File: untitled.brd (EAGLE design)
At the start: 100 x 80 mm, 8 parts

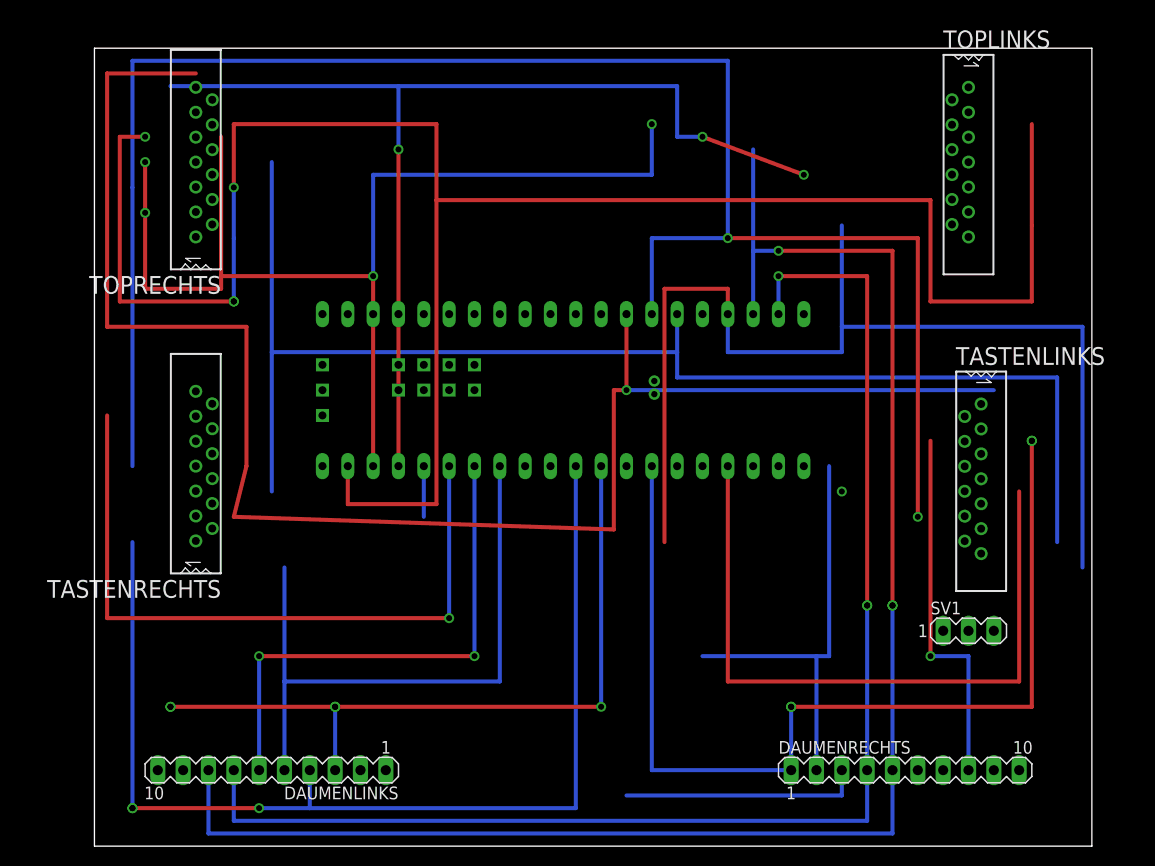
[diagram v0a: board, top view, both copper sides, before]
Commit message: first autorouted version
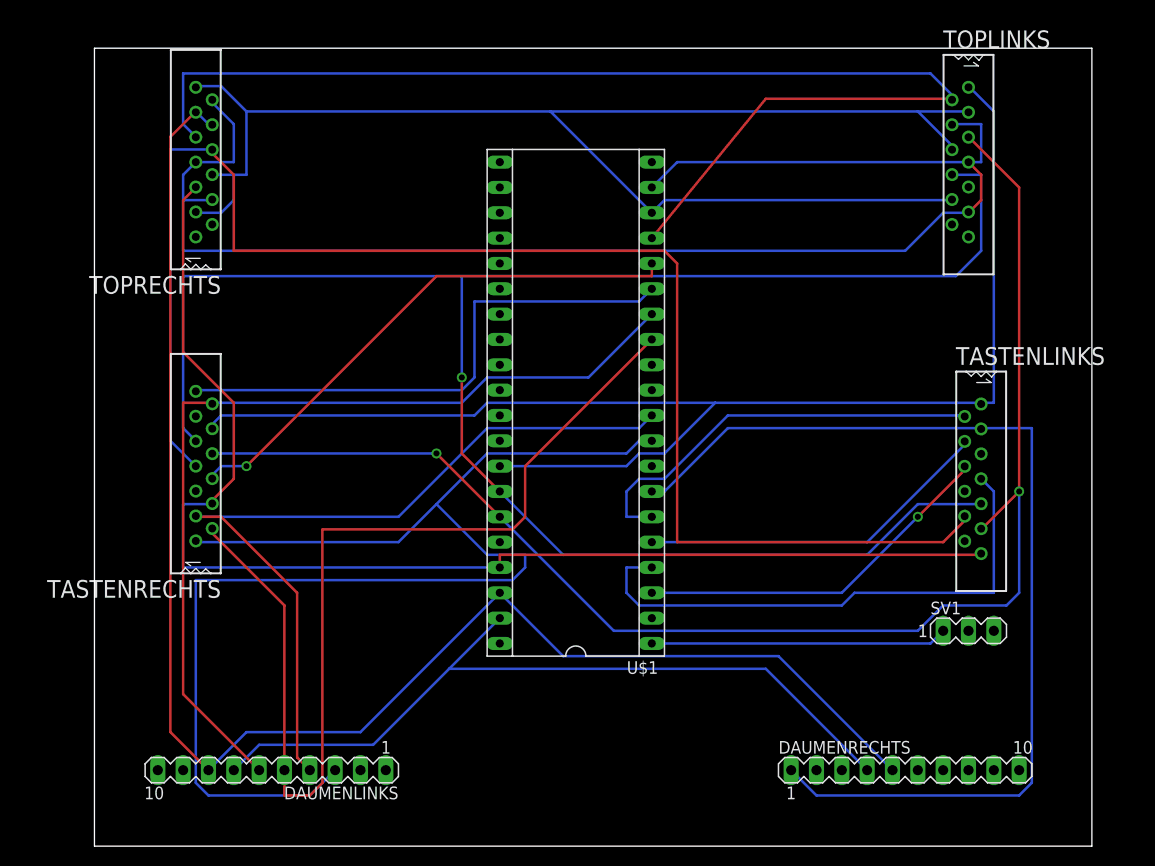
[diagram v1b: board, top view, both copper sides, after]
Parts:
- moved U$1 1.80 mm to (48.3, 44.5), flipped to the top, turned to 90 degrees
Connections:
- net GND: no longer U$1.GND2
- net VCC: no longer U$1.5V
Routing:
- net N$2: track 0.00 -> 152.1 mm
- net D6: track 73.7 -> 131.7 mm, vias 3 -> 0
- net B6: track 135.9 -> 79.1 mm, vias 2 -> 0
- net C6: track 207.0 -> 151.4 mm, vias 3 -> 0
- net C3: track 5.08 -> 54.5 mm, vias 0 -> 1
- net D2: track 43.2 -> 0.00 mm
- net N$16: track 0.00 -> 42.9 mm
- net C0: track 63.5 -> 103.8 mm
- net C1: track 52.1 -> 91.4 mm, vias 2 -> 0
- net N$18: track 0.00 -> 37.4 mm, vias 0 -> 1
- net D3: track 36.8 -> 0.00 mm, vias 1 -> 0
- net N$17: track 0.00 -> 36.3 mm
- net C5: track 113.0 -> 147.7 mm, vias 4 -> 0
- net N$14: track 0.00 -> 29.7 mm
- net B0: track 165.3 -> 137.4 mm, vias 1 -> 0
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
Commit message: board grid set to 1.25mm
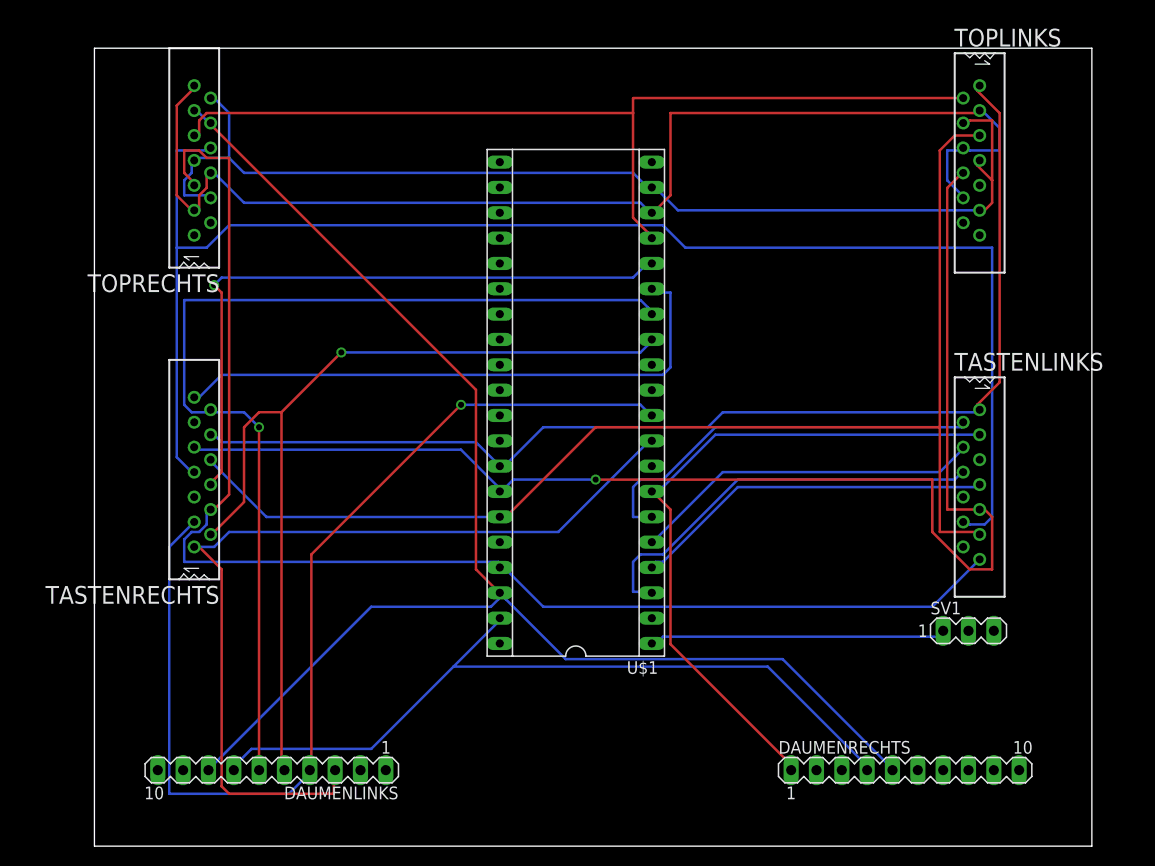
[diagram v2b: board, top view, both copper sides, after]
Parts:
- moved TOPLINKS 1.13 mm to (88.8, 68.8)
- moved TASTENRECHTS 0.62 mm to (10.0, 37.5)
- moved TASTENLINKS 0.60 mm to (88.8, 36.2)
- moved TOPRECHTS 0.23 mm to (10.0, 68.8)
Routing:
- net B1: track 184.9 -> 133.7 mm
- net D6: track 131.7 -> 89.7 mm
- net C6: track 151.4 -> 110.0 mm
- net D4: track 102.1 -> 69.0 mm
- net C4: track 123.3 -> 93.7 mm
- net C5: track 147.7 -> 122.6 mm
- net D7: track 81.7 -> 106.1 mm, vias 0 -> 1
- net B0: track 137.4 -> 115.2 mm
- net D1: track 54.9 -> 36.4 mm
- net B2: track 143.9 -> 126.2 mm, vias 2 -> 0
- net C0: track 103.8 -> 92.7 mm, vias 0 -> 1
- net C3: track 54.5 -> 65.6 mm
- net C1: track 91.4 -> 101.0 mm, vias 0 -> 1
- net B5: track 154.3 -> 144.8 mm
- net B4: track 126.5 -> 135.7 mm
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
